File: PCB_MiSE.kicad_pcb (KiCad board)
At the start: 2 copper layers, 35 parts, among them IC1 MSP430FR2355TPT, J1 WIFI, J2 Conn_01x03, J4 Clk read conn, J6 Display, J7 I2C read, J8 Conn_02x07_Odd_Even, SW1 SW_Push, SW2 SW_Push, SW3 SW_Push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

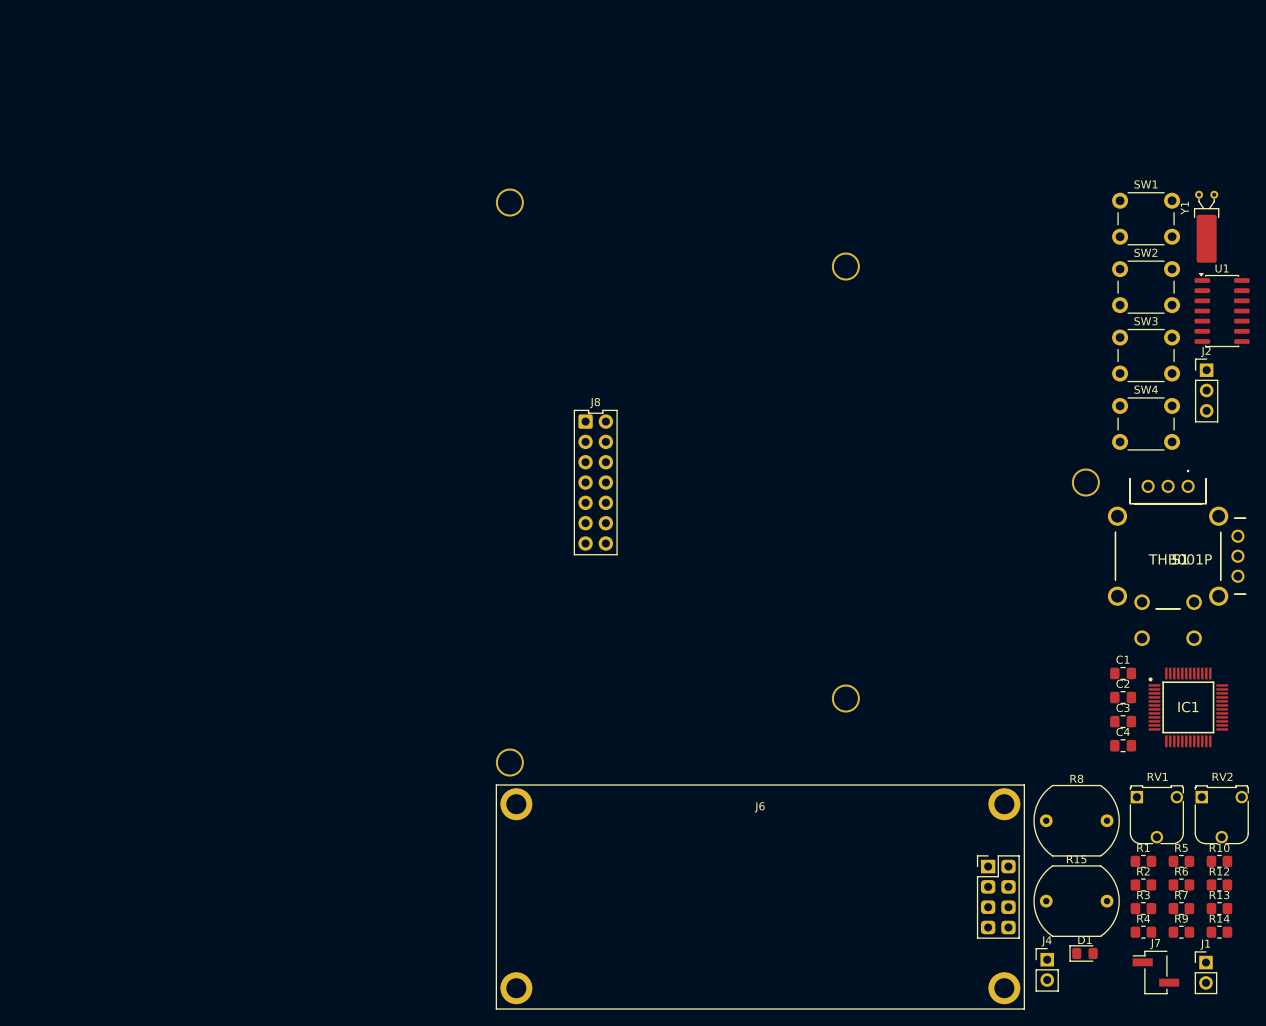
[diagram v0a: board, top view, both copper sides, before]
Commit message: Armo layout de PCB y corrijo errores (no errores DRC)
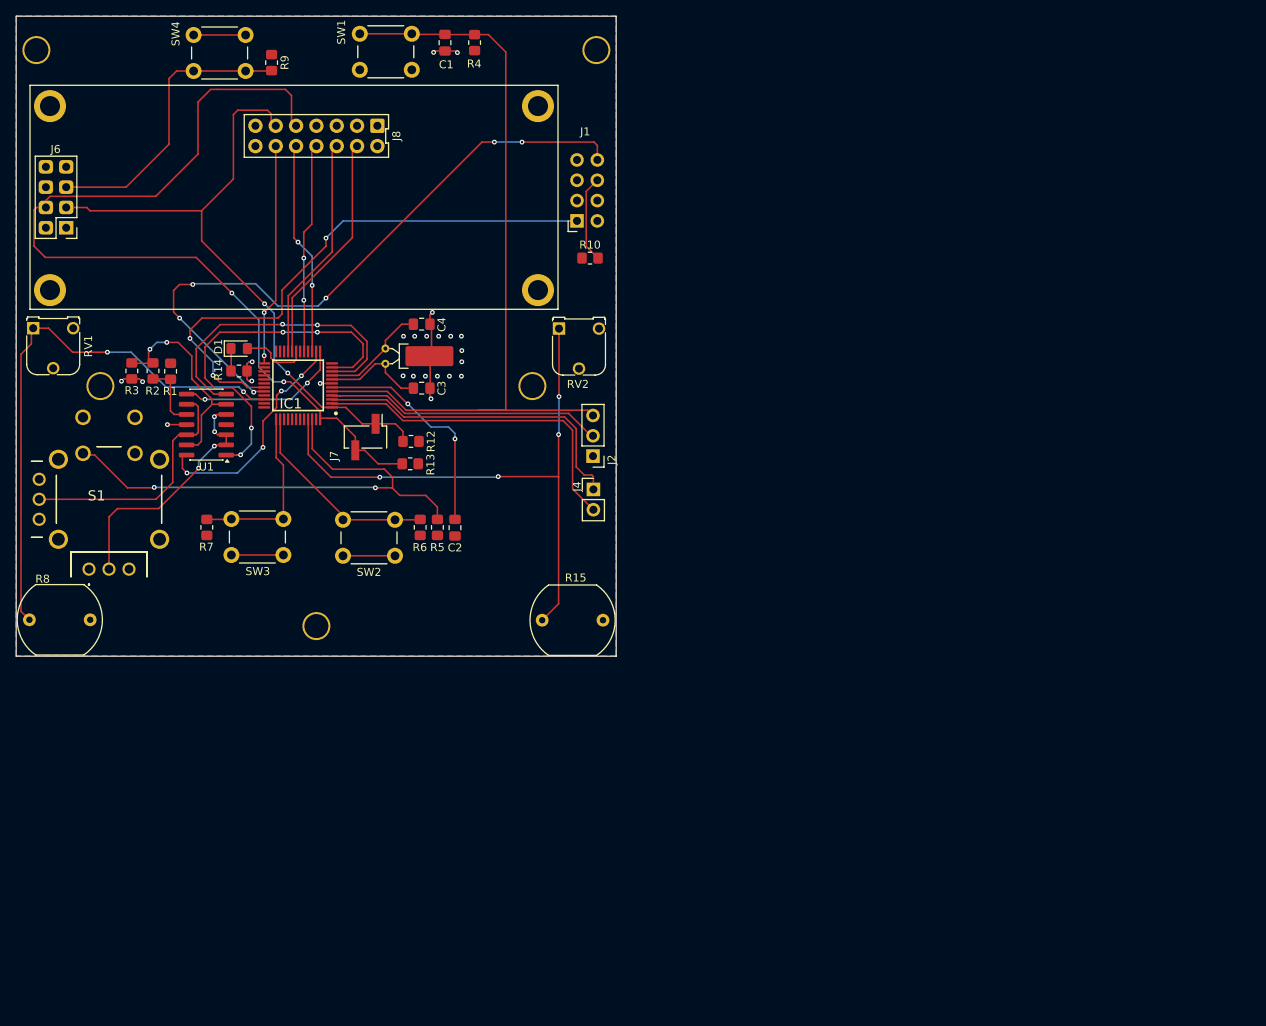
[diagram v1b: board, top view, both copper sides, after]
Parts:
- J1: footprint MSP430:LDR -> Connector_PinSocket_2.54mm:PinSocket_2x04_P2.54mm_Horizontal
- moved R9 157.3 mm to (78.2, 34.6), turned to -90 degrees
- moved RV1 149.9 mm to (48.4, 67.8)
- moved R3 143.2 mm to (60.7, 73.1), turned to -90 degrees
- moved R14 141.2 mm to (74.1, 73.1)
- moved R2 139.5 mm to (63.4, 73.1), turned to 90 degrees
- moved R4 139.1 mm to (103.6, 32.1), turned to 90 degrees
- moved S1 137.8 mm to (55.4, 97.9), turned to 180 degrees
- moved R1 136.2 mm to (65.6, 73.2), turned to -90 degrees
- moved R7 130.8 mm to (70.1, 92.7), turned to 90 degrees
- moved D1 130.0 mm to (74.2, 70.3)
- moved U1 127.8 mm to (70.0, 79.8), turned to 180 degrees
- moved SW4 124.7 mm to (68.5, 31.1)
- moved R8 122.1 mm to (55.5, 104.2), turned to 180 degrees
- moved J1 121.6 mm to (116.4, 54.4), turned to 180 degrees
- moved J7 119.3 mm to (89.9, 81.4), turned to -90 degrees
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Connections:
- net Net-(IC1-P2.6/MCLK/XOUT) renamed C-
- net Net-(IC1-P2.7/TB0CLK/XIN) renamed C+
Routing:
- net SCL: track 0.00 -> 113.8 mm, vias 0 -> 2
- net TDO/TDI: track 0.00 -> 101.2 mm
- net U0TXD: track 0.00 -> 83.2 mm, vias 0 -> 6
- net SDA: track 0.00 -> 80.9 mm, vias 0 -> 2
- net Net-(IC1-P3.2/OA2-): track 0.00 -> 74.4 mm, vias 0 -> 4
- net U0RXD: track 0.00 -> 70.4 mm, vias 0 -> 3
- net Net-(IC1-P1.4/UCA0STE/TCK/A4): track 0.00 -> 70.2 mm, vias 0 -> 2
- net Net-(IC1-P3.1/OA2O): track 0.00 -> 65.4 mm, vias 0 -> 2
- net GPIOr: track 0.00 -> 46.8 mm, vias 0 -> 4
- net GND: track 0.00 -> 44.0 mm, vias 0 -> 10
- net Net-(IC1-P1.1/UCB0CLK/ACLK/OA0O/COMP0.1/A1): track 0.00 -> 42.5 mm
- net Net-(IC1-P1.0/UCB0STE/SMCLK/COMP0.0/A0/VEREF+): track 0.00 -> 41.1 mm
- net GPIOl: track 0.00 -> 38.9 mm, vias 0 -> 2
- net Net-(J6-Pin_5): track 0.00 -> 36.8 mm
- net TCK: track 0.00 -> 34.8 mm
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- added copper zone on B.Cu, net GND
- added copper zone on F.Cu, net VCC
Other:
- board outline added: 75 x 80 mm

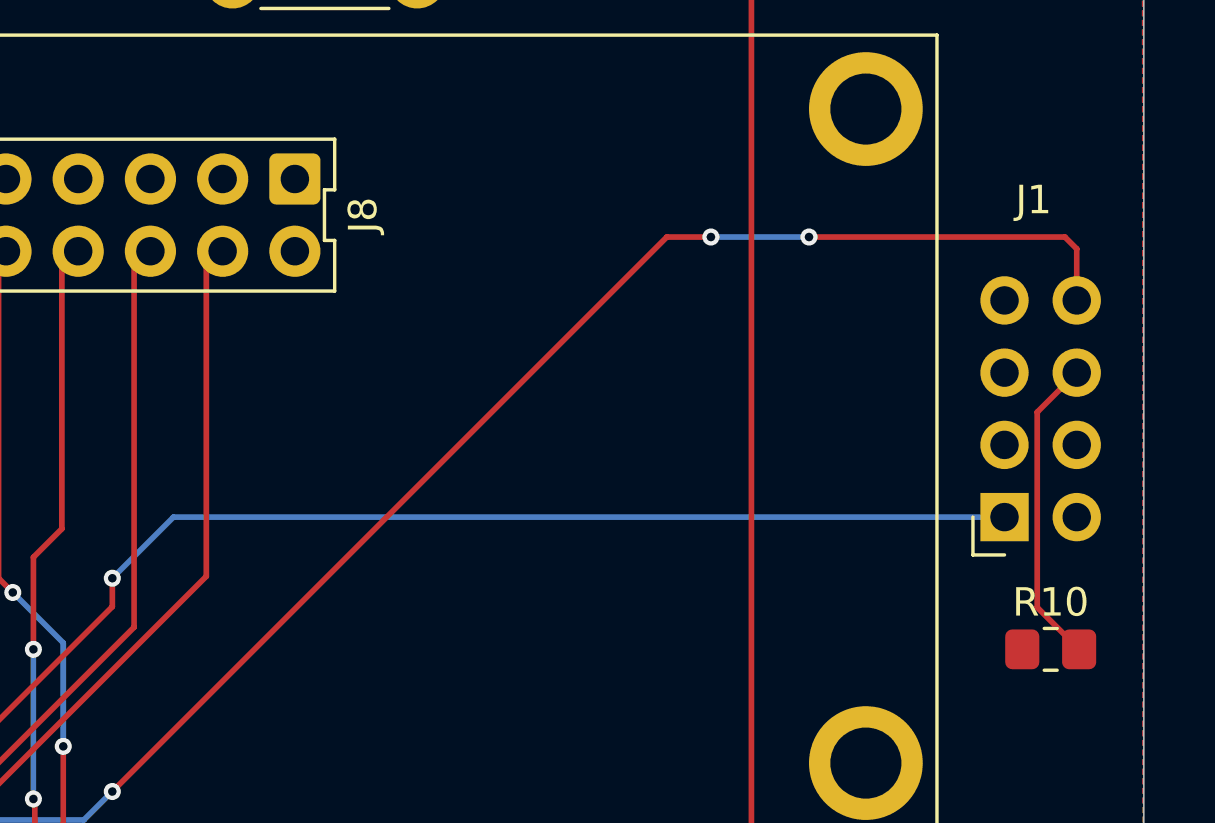
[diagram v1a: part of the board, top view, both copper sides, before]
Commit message: Modifico footprint del wifi
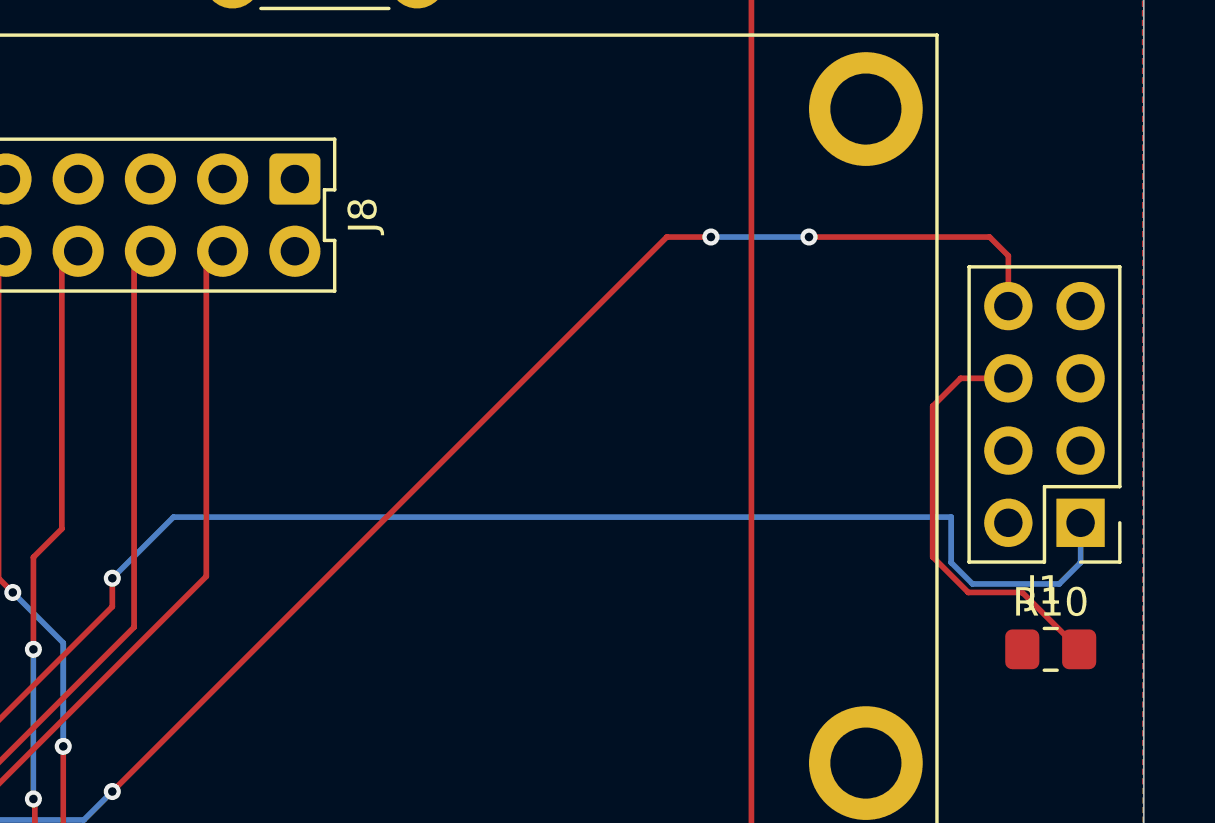
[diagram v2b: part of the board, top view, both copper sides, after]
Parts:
- J1: footprint Connector_PinSocket_2.54mm:PinSocket_2x04_P2.54mm_Horizontal -> Connector_PinHeader_2.54mm:PinHeader_2x04_P2.54mm_Vertical
- moved J1 2.68 mm to (119.0, 54.5)
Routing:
- net U0RXD: track 70.4 -> 76.7 mm
- net CH_EN: track 10.9 -> 14.9 mm
- net U0TXD: track 83.2 -> 80.8 mm

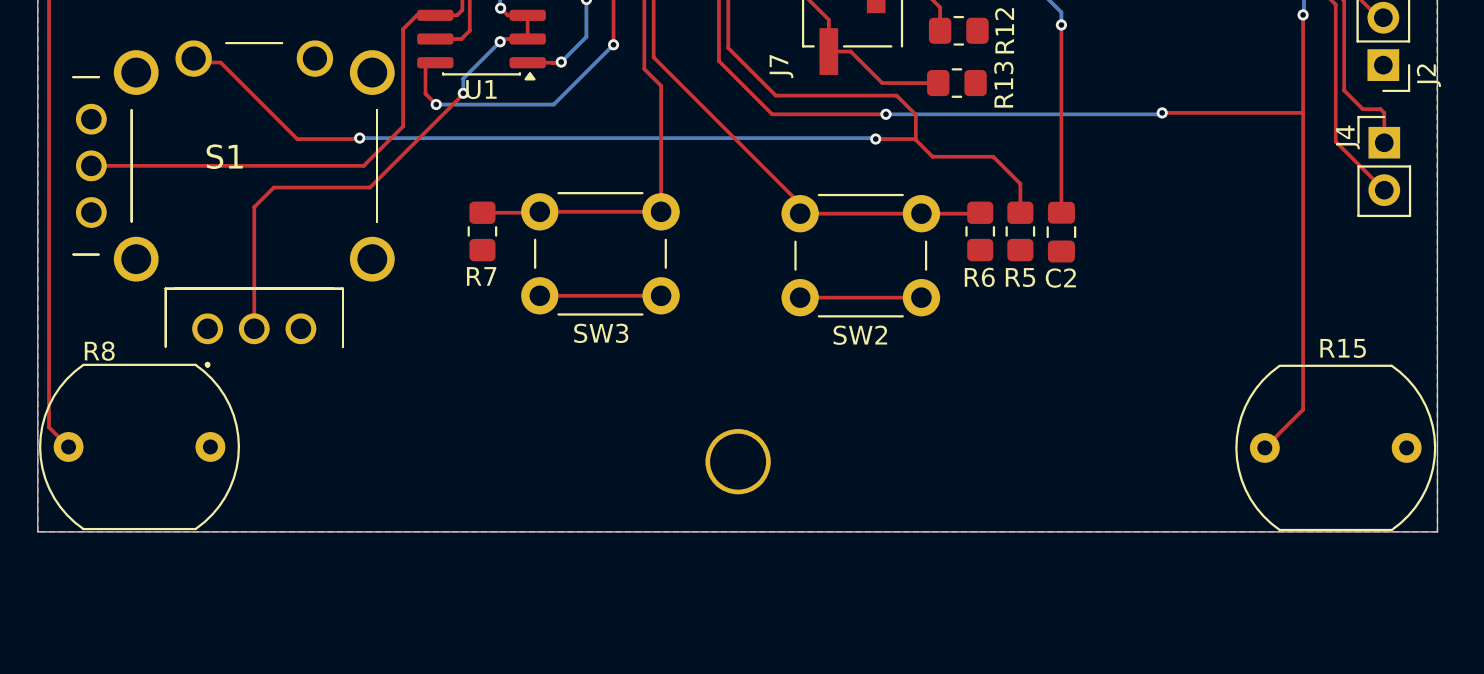
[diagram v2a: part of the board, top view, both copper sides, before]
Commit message: modifico footprints LDRs
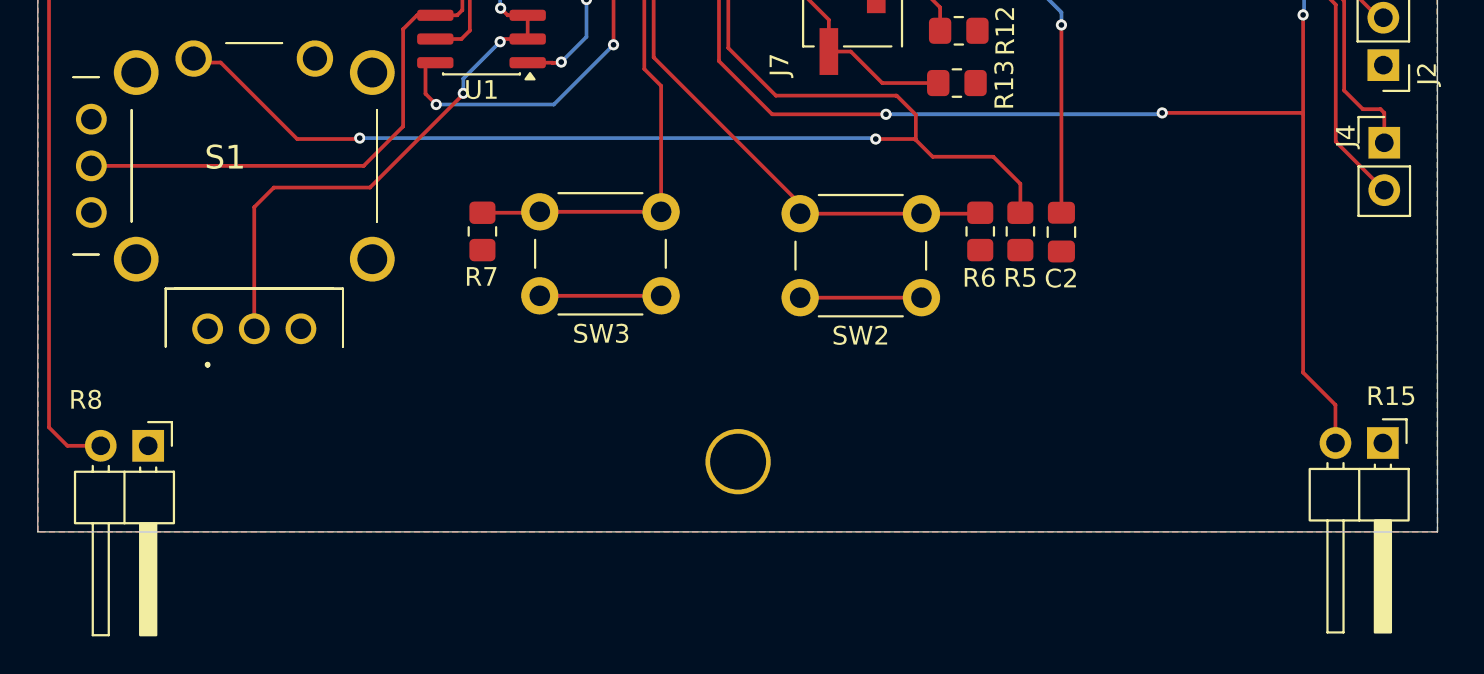
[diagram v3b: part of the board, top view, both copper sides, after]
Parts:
- R15, R8: footprint OptoDevice:R_LDR_10x8.5mm_P7.6mm_Vertical -> Connector_PinHeader_2.54mm:PinHeader_1x02_P2.54mm_Horizontal
- moved R8 3.34 mm to (52.2, 104.2), turned to -90 degrees
- moved R15 1.30 mm to (118.3, 104.0), turned to -90 degrees
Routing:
- net Net-(IC1-P1.4/UCA0STE/TCK/A4): track 70.2 -> 71.9 mm

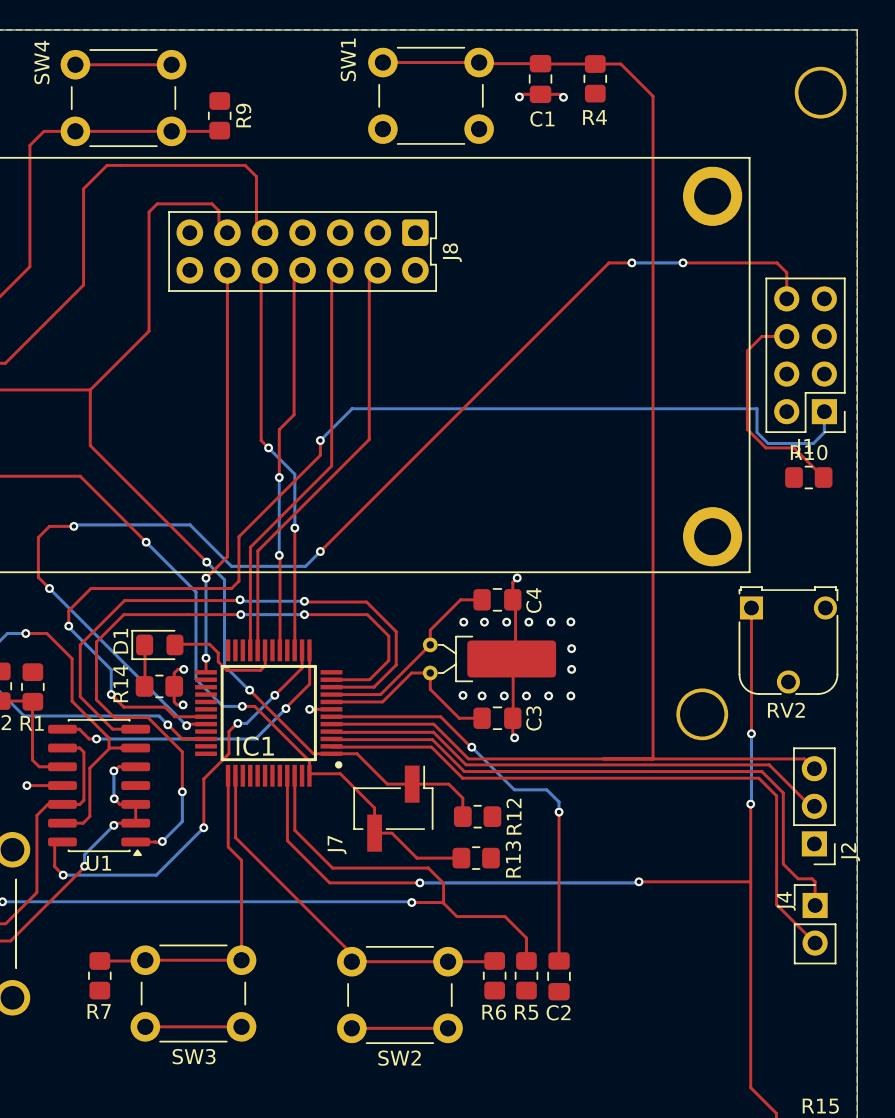
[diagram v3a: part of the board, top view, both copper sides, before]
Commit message: Falta agregar net classes y corregir los errores de diseño
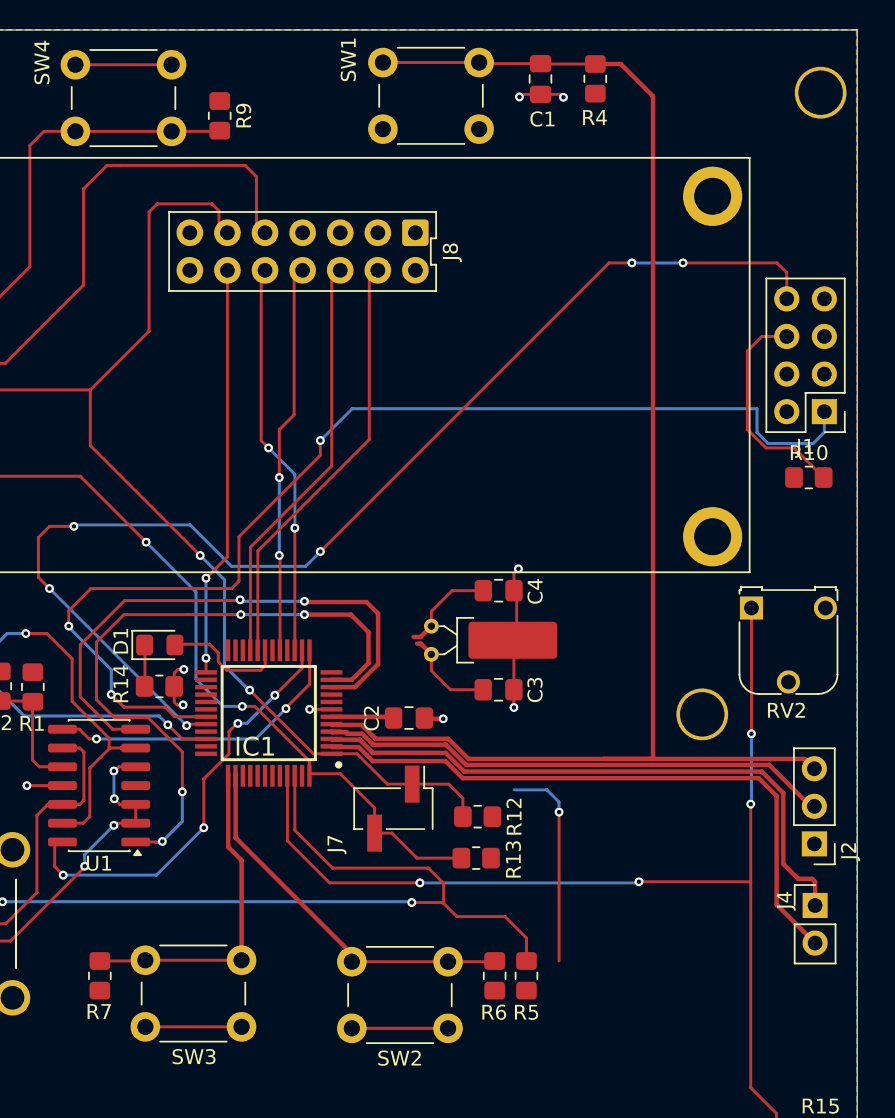
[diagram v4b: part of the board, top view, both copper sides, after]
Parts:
- moved C2 20.2 mm to (91.0, 75.2), turned to 0 degrees
- moved C3 1.93 mm to (97.0, 73.3)
- moved Y1 1.26 mm to (92.5, 70.9)
- moved C4 0.62 mm to (97.0, 66.6)
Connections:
- C2 pad 2: Net-(IC1-DVCC) -> GND
- IC1 pad 6: Net-(IC1-DVCC) -> VCC
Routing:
- net Net-(IC1-DVCC): track 28.5 -> 0.00 mm, vias 2 -> 0
- net VCC: track 0.00 -> 18.4 mm, vias 0 -> 1
- net C-: track 13.4 -> 6.59 mm
- net C+: track 12.9 -> 6.41 mm
- net GPIOr: track 46.8 -> 44.3 mm
- net GPIOl: track 38.9 -> 37.1 mm
- net GND: track 44.0 -> 45.3 mm, vias 10 -> 11
- net (no net): vias 14 -> 0
